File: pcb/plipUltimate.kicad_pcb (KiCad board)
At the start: 2 copper layers, 50 x 50 mm, 55 parts, among them CON1 IEEEE-1284A, CON2 AVR-ISP-6, CON3 RJ45_C, CON4 SD_SPI, CON5 USB_microB, U1 ENC28J60, U2 ATMEGA328P, U3 LM2596_5.0, U4 74LS07, U5 IRF7309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

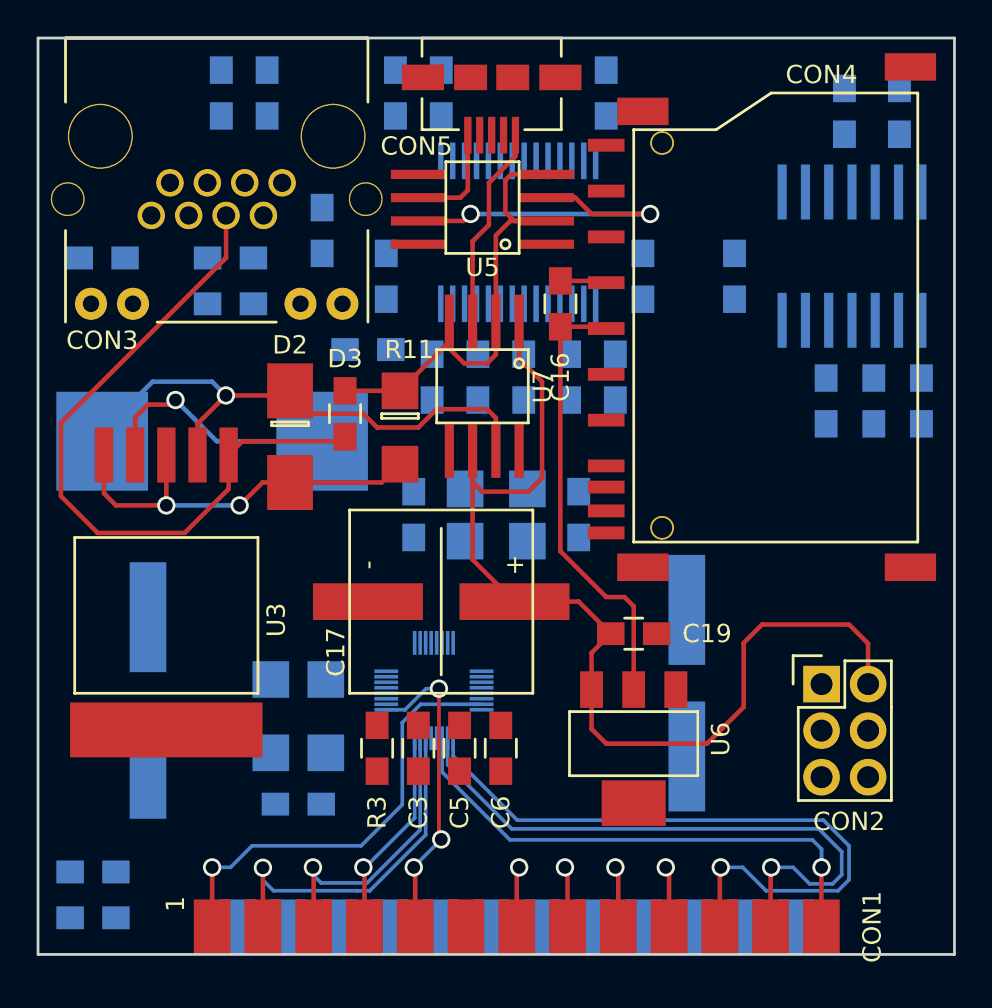
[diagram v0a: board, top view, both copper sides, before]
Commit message: further layout work - 25 connections to go
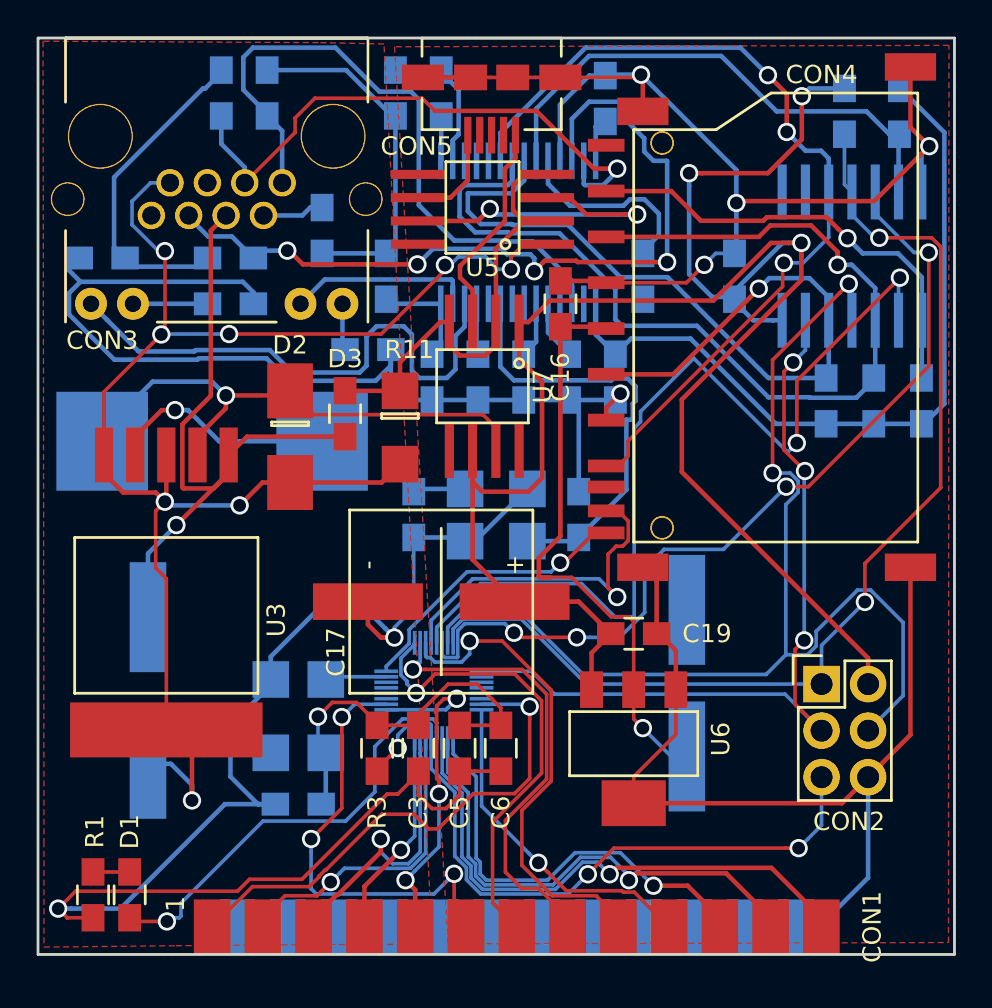
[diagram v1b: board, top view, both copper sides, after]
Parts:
- D1, R1: moved to F.Cu
- moved D1 2.36 mm to (125.0, 86.8), turned to 270 degrees
- moved R1 1.25 mm to (123.0, 86.8), turned to 270 degrees
- moved R2 0.30 mm to (150.9, 43.3)
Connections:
- CON5 pad 6: Net-(CON5-Pad5) -> GND
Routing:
- net GND: track 21.4 -> 298.7 mm, vias 2 -> 9
- net +5V: track 59.3 -> 132.1 mm, vias 0 -> 4
- net +3V3: track 24.6 -> 89.1 mm, vias 0 -> 1
- net AVR_MOSI: track 0.00 -> 62.6 mm, vias 0 -> 2
- net POE_0V: track 23.0 -> 85.1 mm, vias 2 -> 8
- net AVR_MISO: track 0.00 -> 59.2 mm, vias 0 -> 2
- net 3.3V_AVR_MOSI: track 0.00 -> 55.5 mm, vias 0 -> 1
- net SD_CS: track 0.00 -> 50.5 mm, vias 0 -> 2
- net 3.3V_AVR_SCK: track 0.00 -> 47.9 mm, vias 0 -> 1
- net ETH_CS: track 0.00 -> 47.9 mm, vias 0 -> 4
- net 3.3V_AVR_MISO: track 0.00 -> 47.8 mm, vias 0 -> 3
- net Net-(CON3-Pad6): track 0.00 -> 44.7 mm, vias 0 -> 4
- net AVR_SCK: track 0.00 -> 44.1 mm, vias 0 -> 3
- net AVR_RESET: track 0.00 -> 37.7 mm, vias 0 -> 3
- net Net-(CON3-Pad1): track 0.00 -> 35.8 mm
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- added copper zone on F.Cu, net GND
- added copper zone on F.Cu, net POE_0V

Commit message: everything routed!
TODO: home-etching optimizations
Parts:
- moved R4 11.1 mm to (146.2, 44.2), turned to 0 degrees
- moved C2 9.85 mm to (153.0, 49.5), turned to 270 degrees
- moved R3 7.60 mm to (146.1, 77.9), turned to 180 degrees
- moved U2 6.14 mm to (144.7, 80.9)
- moved C1 5.50 mm to (139.8, 53.2), turned to 270 degrees
- moved C5 4.97 mm to (138.8, 81.4)
- moved L1 4.83 mm to (139.8, 48.2)
- moved C4 4.27 mm to (153.0, 54.5), turned to 270 degrees
- moved C6 3.35 mm to (147.3, 81.4)
- moved C3 2.93 mm to (142.1, 81.4)
- moved C7 2.74 mm to (148.8, 57.0), turned to 0 degrees
- moved C14 1.90 mm to (134.8, 80.0), turned to 0 degrees
- moved C17 1.56 mm to (140.9, 69.6)
- moved G1 1.43 mm to (134.8, 75.7), turned to 270 degrees
- moved C9 1.29 mm to (145.1, 59.2), turned to 180 degrees
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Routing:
- net GND: track 298.7 -> 430.3 mm, vias 9 -> 14
- net +3V3: track 89.1 -> 150.2 mm, vias 1 -> 5
- net 3.3V_AVR_MOSI: track 55.5 -> 30.6 mm, vias 1 -> 2
- net Net-(CON3-Pad2): track 3.38 -> 25.1 mm, vias 0 -> 2
- net +5V: track 132.1 -> 149.5 mm, vias 4 -> 6
- net /D5: track 25.8 -> 12.4 mm
- net /D4: track 24.3 -> 11.1 mm, vias 3 -> 1
- net /D6: track 25.0 -> 12.2 mm
- net Net-(CON3-Pad6): track 44.7 -> 56.3 mm, vias 4 -> 2
- net Net-(C10-Pad2): track 2.86 -> 14.0 mm
- net /D3: track 18.4 -> 7.46 mm, vias 3 -> 1
- net Net-(D2-Pad1): track 31.5 -> 42.2 mm
- net AVR_RESET: track 37.7 -> 27.0 mm, vias 3 -> 1
- net 3.3V_AVR_SCK: track 47.9 -> 37.9 mm, vias 1 -> 2
- net Net-(G1-Pad3): track 3.36 -> 12.9 mm
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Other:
- net class Default: clearance 0.2 -> 0.1; trace_width 0.25 -> 0.2
- net class thin removed
- rule trace_clearance: 0.2 -> 0.1

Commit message: Revised schematic, reroute in progress
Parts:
- removed R15, R16: 1k, plipUltimate:0805
- C15, C20, L2: moved to F.Cu
- C17: value 220uF 35V loESR -> 10nF; footprint plipUltimate:electrolyte_SMD -> plipUltimate:0805; moved to B.Cu
- C18: value 10nF -> 220uF 35V loESR; footprint plipUltimate:0805 -> plipUltimate:electrolyte_SMD
- C3, C5, C6, R3: moved to B.Cu
- CON4: value SD_SPI -> USB_microB; footprint plipUltimate:SD-SHORT -> plipUltimate:USB-MicroB
- CON5: value USB_microB -> SD_SPI; footprint plipUltimate:USB-MicroB -> plipUltimate:SD-SHORT
- R1: value 330R -> 820R
- R12: value 1k -> 10k; moved to F.Cu
- R13, R14: value 1k -> 4k7
- U2: footprint plipUltimate:TQFP_32 -> plipUltimate:TQFP-32
- U4: value 74LS07 -> IRF7309; footprint plipUltimate:SO-14 -> plipUltimate:SO-8; moved to F.Cu
- U5: value IRF7309 -> 74LVC125; footprint plipUltimate:SO-8 -> plipUltimate:SO-14; moved to B.Cu
- U6: value AMS1117_3V3 -> IRF7309; footprint plipUltimate:SOT-223 -> plipUltimate:SO-8
- U7: value IRF7309 -> AMS1117_3V3; footprint plipUltimate:SO-8 -> plipUltimate:SOT-223
- moved C8 96.9 mm to (84.2, 120.8), turned to 90 degrees
- moved R13 96.7 mm to (106.2, 119.2), turned to 0 degrees
- moved R4 95.5 mm to (80.5, 113.5), turned to 90 degrees
- moved R2 92.6 mm to (83.5, 106.8), turned to 0 degrees
- moved C2 86.7 mm to (88.5, 107.5), turned to 0 degrees
- moved R12 86.7 mm to (106.0, 108.5), turned to 0 degrees
- moved U1 85.7 mm to (88.2, 113.8), turned to 90 degrees
- moved C1 84.8 mm to (88.2, 120.5), turned to 0 degrees
- moved R14 84.1 mm to (106.2, 116.8), turned to 0 degrees
- moved U4 80.1 mm to (104.2, 106.3), turned to 90 degrees
- moved D2 78.9 mm to (82.0, 121.2)
- moved C4 78.7 mm to (96.8, 109.5), turned to 180 degrees
- moved CON5 78.2 mm to (111.5, 115.8), turned to 90 degrees
- moved C7 76.3 mm to (96.8, 112.8), turned to 180 degrees
- moved C9 74.6 mm to (96.8, 116.0)
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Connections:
- C17 pad 1: +5V -> +3V3
- C18 pad 1: GND -> +5V
- C18 pad 2: +5V -> GND
- CON4 pad 1: 3.3V_SD_CS -> Net-(CON4-Pad1)
- CON4 pad 2: 3.3V_AVR_MOSI -> Net-(CON4-Pad2)
- CON4 pad 3: GND -> Net-(CON4-Pad3)
- CON4 pad 4: +3V3 -> Net-(CON4-Pad4)
- CON4 pad 5: 3.3V_AVR_SCK -> Net-(CON4-Pad5)
- CON5 pad 1: Net-(CON5-Pad1) -> 3.3V_SD_CS
- CON5 pad 2: Net-(CON5-Pad2) -> 3.3V_AVR_MOSI
- CON5 pad 3: Net-(CON5-Pad3) -> GND
- CON5 pad 4: Net-(CON5-Pad4) -> +3V3
- CON5 pad 5: Net-(CON5-Pad5) -> 3.3V_AVR_SCK
- R12 pad 1: +5V -> POE_0V
- R12 pad 2: AVR_MISO -> Net-(D3-Pad1)
- R13 pad 1: +3V3 -> +5V
- R13 pad 2: 3.3V_ETH_CS -> SD_DETECT
- R14 pad 1: +3V3 -> +5V
- R14 pad 2: 3.3V_SD_CS -> SD_LOCK
- U1 pad 6: 3.3V_AVR_MISO -> AVR_MISO
- U1 pad 7: 3.3V_AVR_MOSI -> AVR_MOSI
- U1 pad 8: 3.3V_AVR_SCK -> AVR_SCK
- U1 pad 9: 3.3V_ETH_CS -> ETH_CS
- U4 pad 1: Net-(U4-Pad1) -> POE_0V
- U4 pad 2: Net-(U4-Pad2) -> Net-(D3-Pad1)
- U4 pad 3: 3.3V_AVR_MISO -> GND
- U4 pad 4: AVR_MISO -> Net-(D3-Pad1)
- U4 pad 5: ETH_CS -> (no net)
- U4 pad 6: 3.3V_ETH_CS -> Net-(CON4-Pad5)
- U4 pad 8: 3.3V_SD_CS -> (no net)
- U5 pad 1: POE_0V -> GND
- U5 pad 2: Net-(D3-Pad1) -> Net-(U5-Pad2)
- U5 pad 3: GND -> Net-(U5-Pad3)
- U5 pad 4: Net-(D3-Pad1) -> GND
- U5 pad 5: (no net) -> SD_CS
- U5 pad 6: Net-(CON5-Pad5) -> 3.3V_SD_CS
- U5 pad 8: (no net) -> 3.3V_AVR_MOSI
- U6 pad 1: GND -> +5V
- U6 pad 2: +3V3 -> Net-(D3-Pad1)
- U6 pad 3: +5V -> Net-(CON4-Pad1)
- U7 pad 1: +5V -> GND
- U7 pad 2: Net-(D3-Pad1) -> +3V3
- U7 pad 3: Net-(CON5-Pad1) -> +5V
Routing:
- net +3V3: track 150.2 -> 68.0 mm, vias 5 -> 0
- net AVR_MISO: track 58.9 -> 0.00 mm, vias 2 -> 0
- net 3.3V_AVR_MISO: track 51.6 -> 0.00 mm, vias 2 -> 0
- net ETH_CS: track 51.5 -> 0.00 mm, vias 3 -> 0
- net 3.3V_AVR_SCK: track 37.9 -> 0.00 mm, vias 2 -> 0
- net Net-(CON3-Pad6): track 56.3 -> 18.8 mm, vias 2 -> 0
- net AVR_MOSI: track 56.5 -> 24.4 mm, vias 2 -> 0
- net 3.3V_ETH_CS: track 31.7 -> 0.00 mm, vias 2 -> 0
- net SD_CS: track 45.2 -> 14.4 mm
- net 3.3V_AVR_MOSI: track 30.6 -> 0.00 mm, vias 2 -> 0
- net AVR_SCK: track 45.4 -> 18.7 mm, vias 3 -> 0
- net /~STROBE: track 26.6 -> 0.00 mm, vias 1 -> 0
- net GND: track 430.3 -> 404.5 mm, vias 14 -> 0
- net Net-(CON3-Pad12): track 25.2 -> 0.00 mm
- net 3.3V_SD_CS: track 24.0 -> 0.00 mm, vias 1 -> 0
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- added copper zone on B.Cu, net GND
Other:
- net class Default: clearance 0.1 -> 0.3; trace_width 0.2 -> 0.3; via_dia 1 -> 1.5; via_drill 0.7 -> 0.3
- rule pad_to_mask_clearance: 0.2 -> 0
- rule trace_clearance: 0.1 -> 0.3
- rule via_min_size: 1 -> 0.4
- board text added: "BS: Children of the grave Rev. 2"
- board text added: "github.com/tehKaiN/plipUltimate"

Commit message: Complete rev 2 sch and PCB
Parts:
- removed C20: 47uF 6,3V, plipUltimate:electrolyte_SMD
- removed C5: 100nF, plipUltimate:0805
- C17, C3, C6, C8, U2: moved to F.Cu
- C19: value 100nF -> 10uF 6,3V
- D3, L2, R11, R12, U6: moved to B.Cu
- U4: value IRF7309 -> 74LVC125; footprint plipUltimate:SO-8 -> plipUltimate:SO-14
- U5: value 74LVC125 -> IRF7309; footprint plipUltimate:SO-14 -> plipUltimate:SO-8
- moved D1 73.2 mm to (54.9, 132.0), turned to 90 degrees
- moved R1 73.1 mm to (52.5, 132.0), turned to 90 degrees
- moved C6 51.4 mm to (68.4, 121.0)
- moved L1 50.5 mm to (53.2, 86.7), turned to 180 degrees
- moved U7 48.8 mm to (75.2, 98.4), turned to 180 degrees
- moved C11 47.3 mm to (53.6, 113.6), turned to 0 degrees
- moved R5 44.7 mm to (56.6, 90.2), turned to 270 degrees
- moved U5 44.5 mm to (76.0, 97.8)
- moved X1 43.4 mm to (53.4, 118.1)
- moved R6 43.2 mm to (58.8, 90.2), turned to 270 degrees
- moved U3 41.8 mm to (54.4, 107.8), turned to 90 degrees
- moved C12 41.7 mm to (60.0, 86.6), turned to 180 degrees
- moved R3 41.6 mm to (78.2, 127.4), turned to 90 degrees
- moved C19 41.3 mm to (76.4, 94.6), turned to 0 degrees
- moved C10 39.6 mm to (53.4, 122.3), turned to 180 degrees
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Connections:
- net Net-(C10-Pad2) renamed /OSC2
- net Net-(C11-Pad2) renamed /OSC1
- net Net-(CON3-Pad1) renamed /TX+
- net Net-(CON3-Pad2) renamed /TX-
- net Net-(CON3-Pad3) renamed /RX+
- net Net-(CON3-Pad6) renamed /RX-
- net Net-(G1-Pad3) renamed /AVR_CLK
- C19 pad 1: +5V -> +3V3
- CON3 pad 11: Net-(CON3-Pad11) -> GND
- CON3 pad 9: Net-(CON3-Pad9) -> GND
- R10 pad 1: Net-(CON3-Pad11) -> Net-(CON3-Pad12)
- R10 pad 2: GND -> /LEDB
- R9 pad 1: Net-(CON3-Pad9) -> Net-(CON3-Pad10)
- R9 pad 2: GND -> /LEDA
- U1 pad 26: Net-(CON3-Pad12) -> /LEDB
- U1 pad 27: Net-(CON3-Pad10) -> /LEDA
- U4 pad 1: POE_0V -> GND
- U4 pad 2: Net-(D3-Pad1) -> GND
- U4 pad 3: GND -> Net-(U4-Pad3)
- U4 pad 4: Net-(D3-Pad1) -> GND
- U4 pad 5: (no net) -> SD_CS
- U4 pad 6: Net-(CON4-Pad5) -> 3.3V_SD_CS
- U4 pad 8: (no net) -> 3.3V_AVR_MOSI
- U5 pad 1: GND -> POE_0V
- U5 pad 2: Net-(U5-Pad2) -> Net-(D3-Pad1)
- U5 pad 3: Net-(U5-Pad3) -> GND
- U5 pad 4: GND -> Net-(D3-Pad1)
- U5 pad 5: SD_CS -> (no net)
- U5 pad 6: 3.3V_SD_CS -> Net-(CON4-Pad5)
- U5 pad 8: 3.3V_AVR_MOSI -> (no net)
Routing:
- net +3V3: track 68.0 -> 209.0 mm, vias 0 -> 9
- net AVR_MISO: track 0.00 -> 63.2 mm, vias 0 -> 2
- net POE_0V: track 101.0 -> 41.5 mm, vias 0 -> 1
- net GND: track 404.5 -> 453.4 mm, vias 0 -> 13
- net AVR_SCK: track 18.7 -> 65.9 mm, vias 0 -> 2
- net AVR_MOSI: track 24.4 -> 69.2 mm, vias 0 -> 1
- net 3.3V_SD_CS: track 0.00 -> 44.7 mm, vias 0 -> 2
- net /POUT: track 0.00 -> 34.7 mm, vias 0 -> 2
- net SD_DETECT: track 3.12 -> 37.7 mm, vias 0 -> 3
- net /SEL: track 0.00 -> 34.4 mm, vias 0 -> 2
- net /BUSY: track 0.00 -> 33.6 mm, vias 0 -> 2
- net /~ACK: track 0.00 -> 31.6 mm, vias 0 -> 2
- net 3.3V_AVR_MOSI: track 0.00 -> 29.3 mm
- net /LEDA: track 0.00 -> 27.6 mm, vias 0 -> 2
- net /D7: track 0.00 -> 27.2 mm
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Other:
- net class Default: clearance 0.3 -> 0.25; trace_width 0.3 -> 0.25
- rule trace_clearance: 0.3 -> 0.25
- rule via_min_size: 0.4 -> 1.5
- board text added: "Children of the Grave plipUltimate Rev. 2"
- board text removed: "BS: Children of the grave Rev. 2"
- board text removed: "github.com/tehKaiN/plipUltimate"

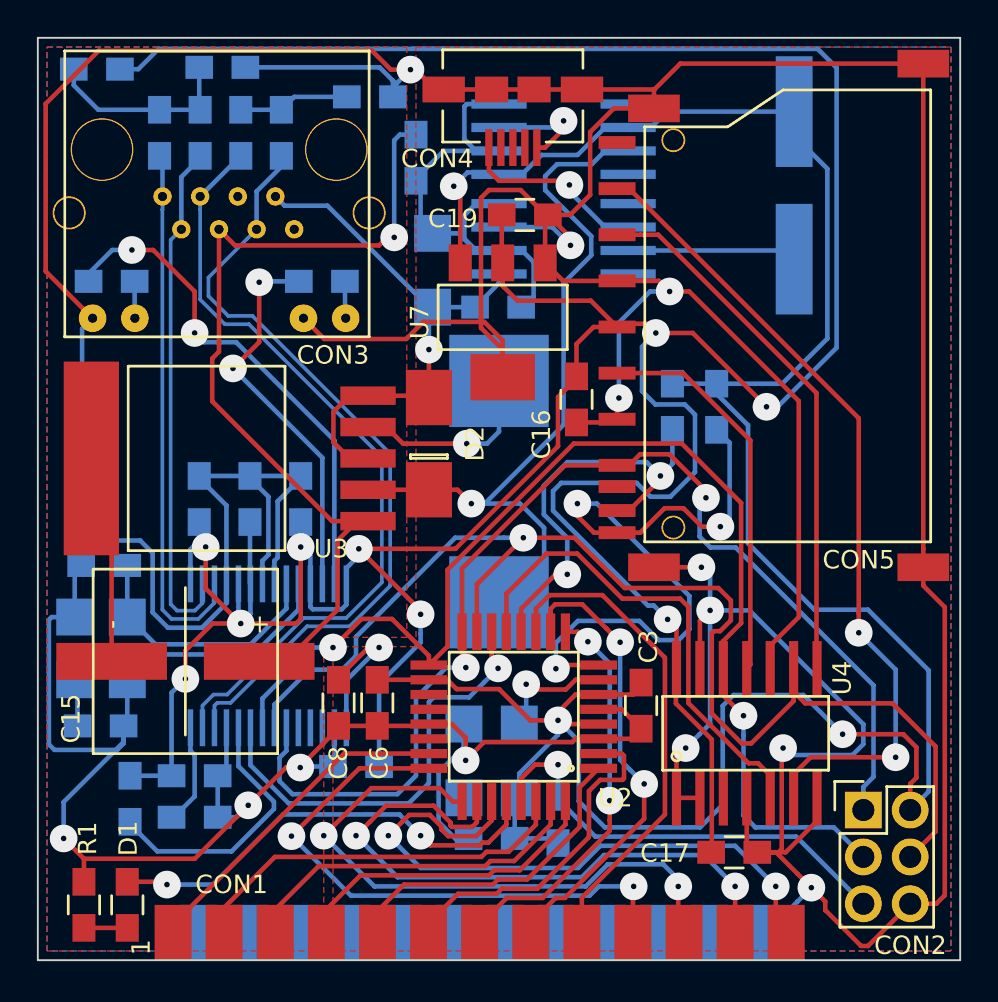
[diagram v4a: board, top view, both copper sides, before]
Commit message: minor pcb fixes
TODO: 20MHz & SD footprints are broken
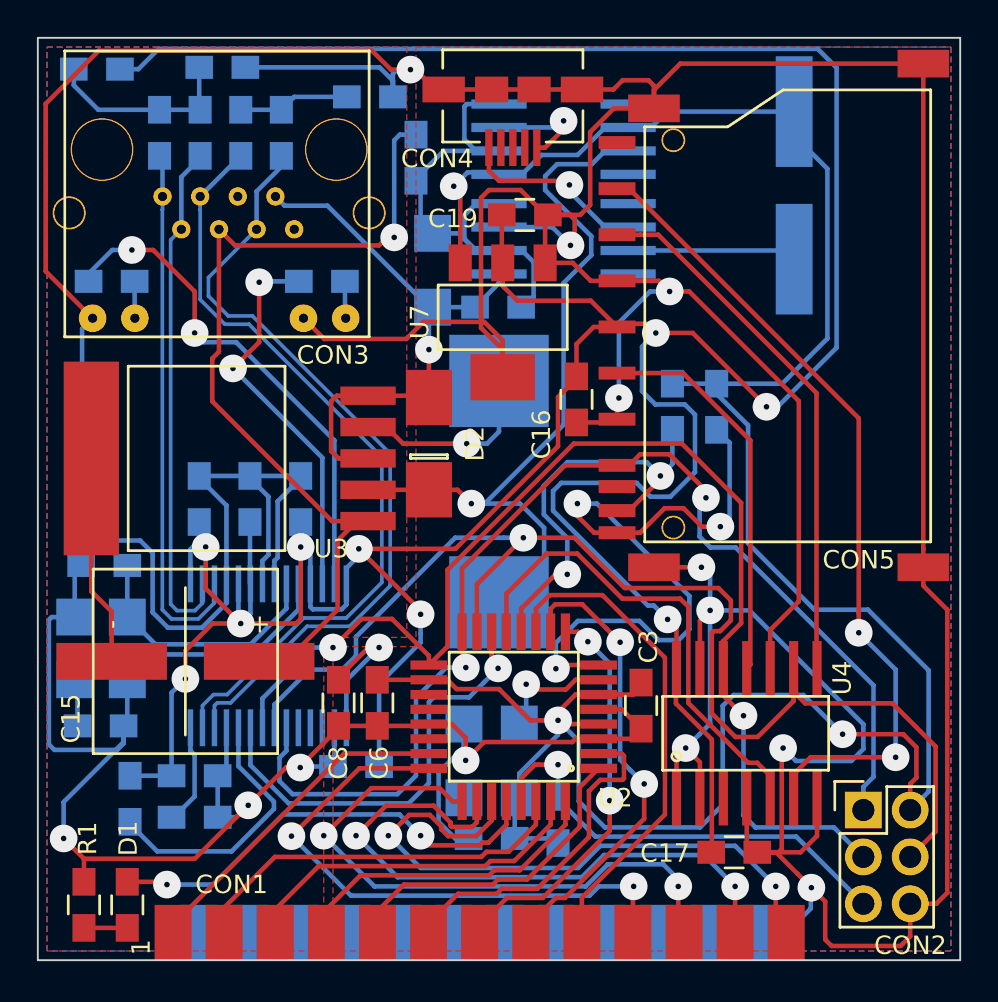
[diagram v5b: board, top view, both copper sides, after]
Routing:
- net GND: track 453.4 -> 461.3 mm
- net POE_0V: track 41.5 -> 42.4 mm

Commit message: further layout optimizations
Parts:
- moved G1 1.80 mm to (74.7, 122.4)
- moved R12 1.75 mm to (76.7, 99.6)
- moved CON4 1.66 mm to (76.0, 89.0)
- moved R11 0.98 mm to (71.4, 91.1)
- moved U3 0.50 mm to (54.4, 107.3)
- moved C14 0.32 mm to (74.7, 128.7)
- moved R3 0.30 mm to (78.5, 127.4)
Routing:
- net POE_0V: track 42.4 -> 47.1 mm
- net GND: track 461.3 -> 465.9 mm
- net +3V3: track 209.0 -> 206.7 mm
- net AVR_MISO: track 63.2 -> 65.2 mm
- net +5V: track 140.8 -> 142.5 mm
- net /D5: track 22.3 -> 23.7 mm
- net ETH_CS: track 24.0 -> 25.4 mm
- net SD_DETECT: track 37.7 -> 38.7 mm
- net Net-(CON4-Pad1): track 5.96 -> 4.98 mm
- net Net-(CON4-Pad5): track 10.3 -> 11.2 mm
- net /LEDA: track 27.6 -> 26.7 mm
- net /~ACK: track 31.6 -> 32.5 mm
- net /SEL: track 34.4 -> 35.2 mm
- net /POUT: track 34.7 -> 35.6 mm
- net Net-(D2-Pad1): track 42.4 -> 43.2 mm
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
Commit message: minor layout tweaks
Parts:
- moved CON1 0.20 mm to (57.3, 133.3)
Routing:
- net GND: track 465.9 -> 468.3 mm
- net /D0: track 21.3 -> 22.0 mm
